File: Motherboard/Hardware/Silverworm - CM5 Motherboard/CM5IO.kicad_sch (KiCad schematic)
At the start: 12 parts, among them J11 USB_C_Receptacle_USB2.0

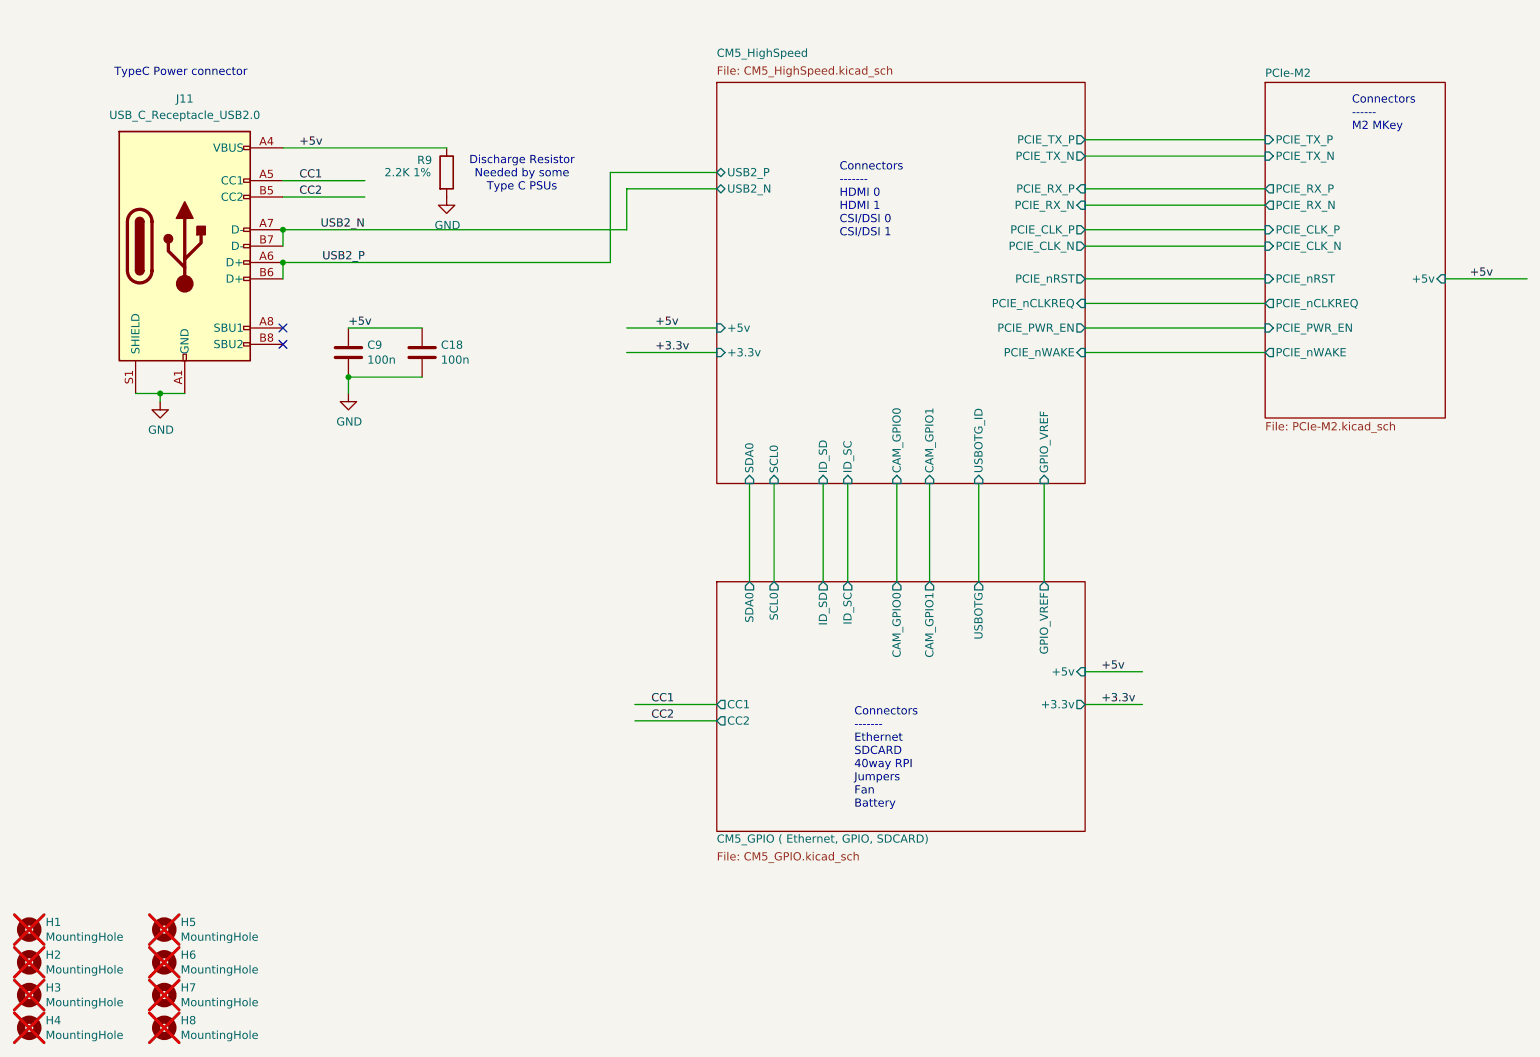
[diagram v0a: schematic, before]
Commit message: Motherboard schematics edits
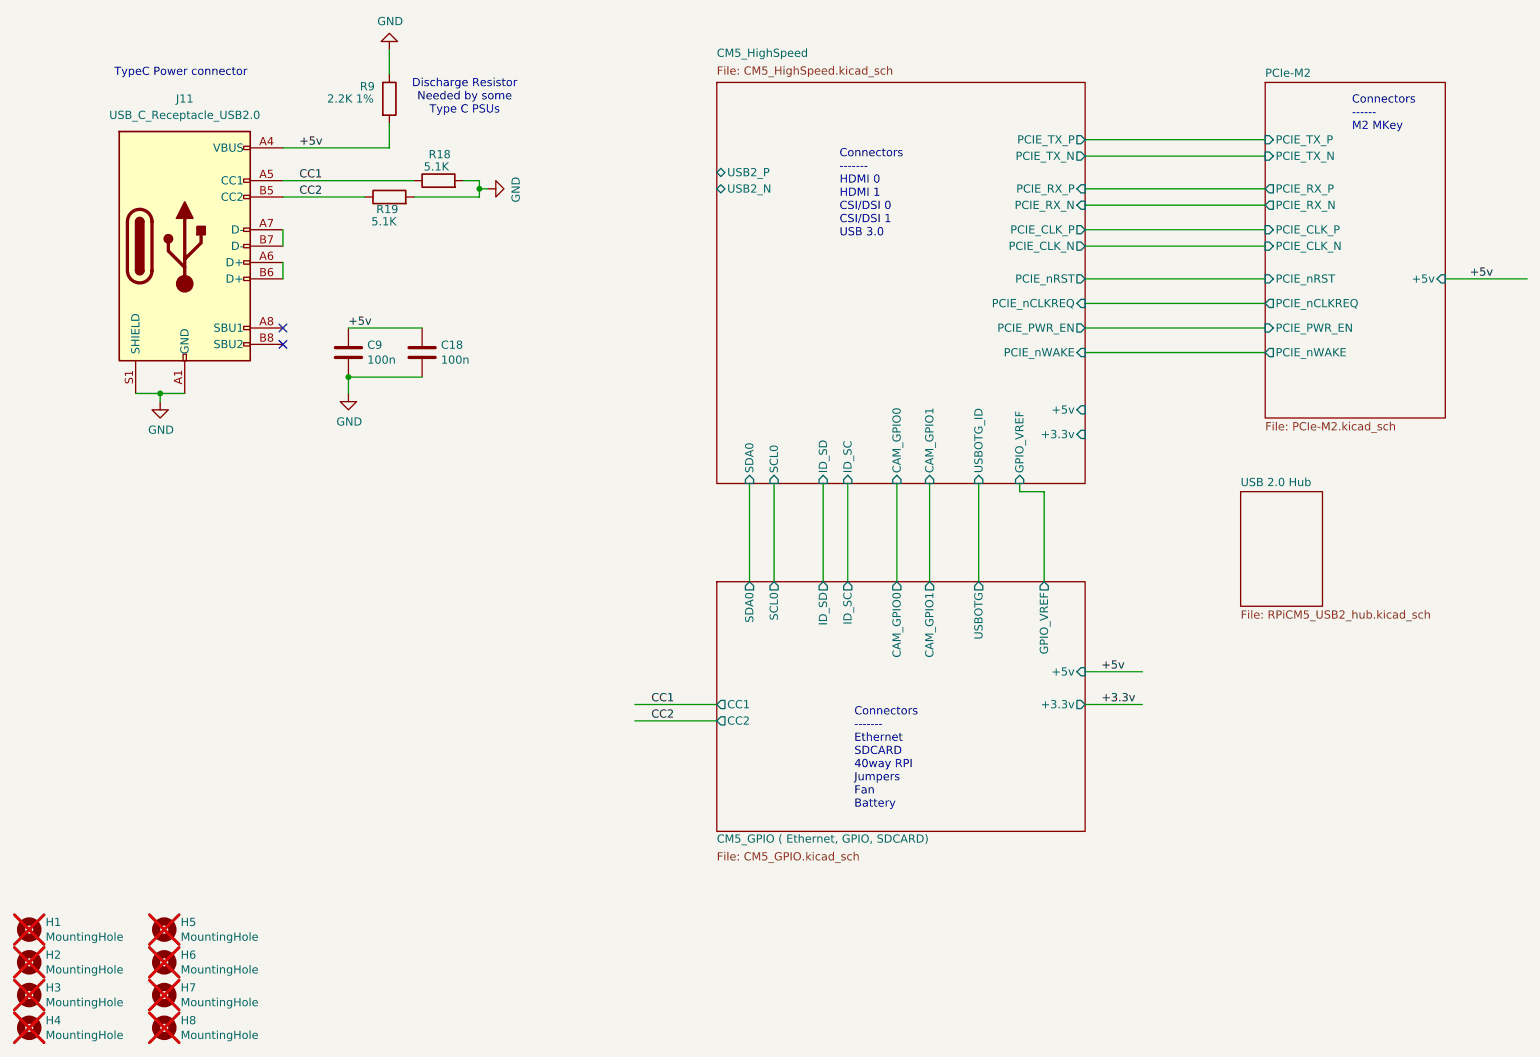
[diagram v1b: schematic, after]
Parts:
- added R18, R19: 5.1K, Resistor_SMD:R_0402_1005Metric, symbol Device:R
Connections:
- net +5v: now also R9.2; no longer R9.1
- net CC1: now also R18.1
- net CC2: now also R19.1
- net GND: now also R9.1, R18.2, R19.2; no longer R9.2
- net USB2_N: no longer names the net of J11.A7 (D-), J11.B7 (D-)
- net USB2_P: no longer names the net of J11.A6 (D+), J11.B6 (D+)
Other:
- added sheet USB 2.0 Hub (RPiCM5_USB2_hub.kicad_sch)
- note added: "Connectors ------- HDMI 0 HDMI 1 CSI/DSI 0 CSI/DSI 1 USB 3.0"
- note removed: "Connectors ------- HDMI 0 HDMI 1 CSI/DSI 0 CSI/DSI 1"
- company: Copyright © 2024 Raspberry Pi Ltd. -> Copyright © Zak Leek, Imperial College London
- title: Compute Module 5 IO Board - Top Level -> Silverworm CM5 Motherboard - Top Level
- moved on the sheet: R9
